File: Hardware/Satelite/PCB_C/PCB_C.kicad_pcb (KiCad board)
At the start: 2 copper layers, 54 x 54 mm, 54 parts, among them IC1 MCP1501T-33E_CHY, IC2 IS25LP080D-JULE-TR, IC3 BQ24392RSER, IC4 MS563702BA03-50, IC5 BMX055, J1 Conn_01x06, J2 BOOT, J3 Conector_PCB_B-C, J4 Conector_Expansion_CanSat, J5 USB_B_Micro, M1 Spacer, M2 Spacer, M3 Spacer, Q1 BC817, U1 NTB0104BQ,115, U2 TCA9802DGKR, U3 STM32F303RETx, U4 NTB0104BQ,115, U5 SN74LVC1G3157DCKR, U6 Si7006-A20-IM1, Y1 LFXTAL016178, Y2 Crystal

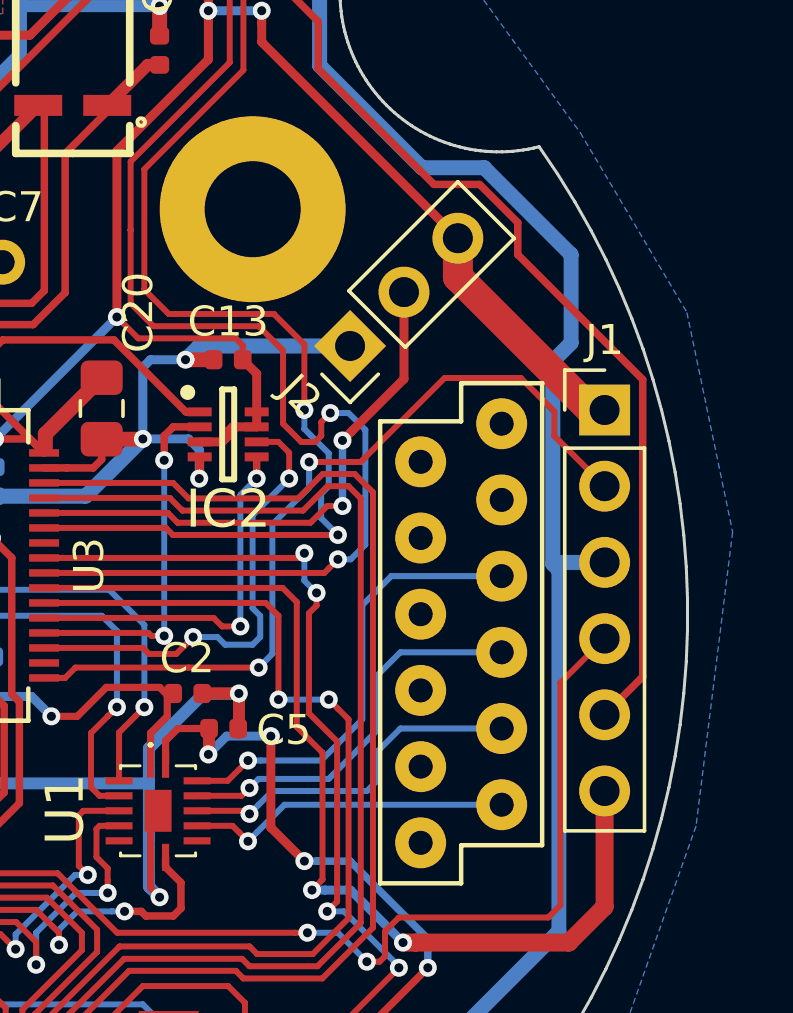
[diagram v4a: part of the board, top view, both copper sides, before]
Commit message: Header de programacion y BOOT de PCB pasados a bottom
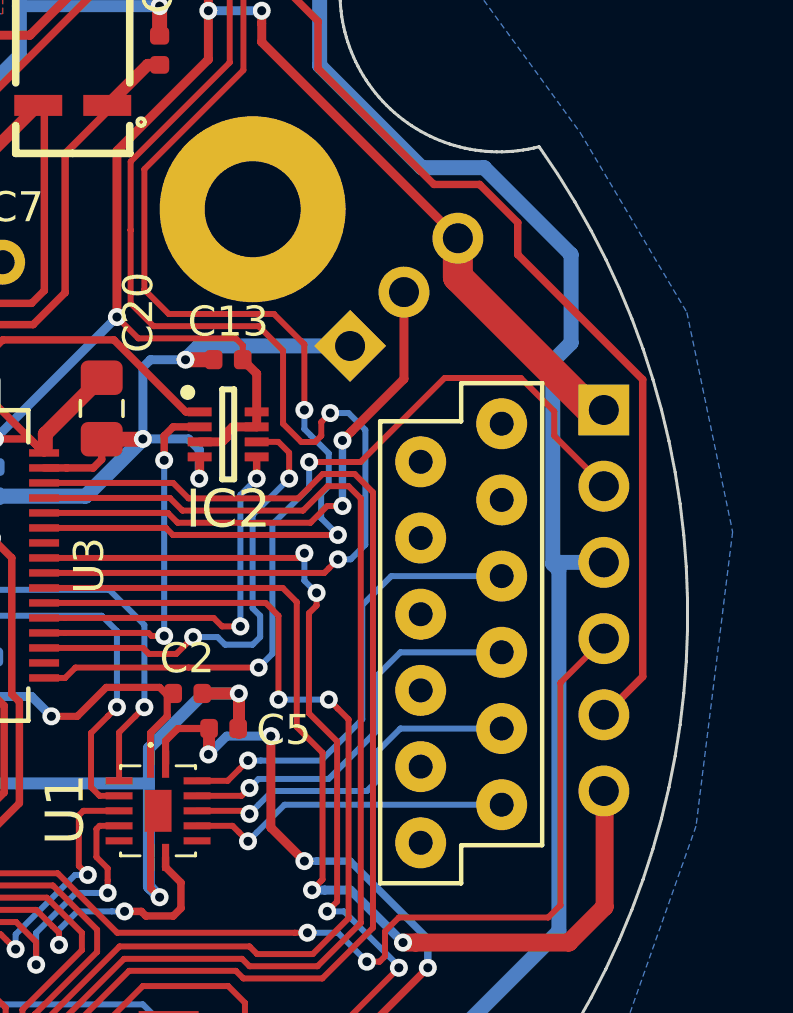
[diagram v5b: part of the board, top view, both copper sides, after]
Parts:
- J1, J2: moved to B.Cu
- turned J1 to 180 degrees
- turned J2 to 315 degrees
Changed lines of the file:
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@@
       (net 27 /IMU/ACC_INT))
   )
-  (module Connector_PinHeader_2.54mm:PinHeader_1x06_P2.54mm_Vertical (layer F.Cu)
-    (at 24.2316 -6.8072)
+  (module Connector_PinHeader_2.54mm:PinHeader_1x06_P2.54mm_Vertical (layer B.Cu)
+    (at 24.2062 -6.8072 180)
     (descr "Through hole straight pin header, 1x06, 2.54mm pitch, single row")
     (tags "Through hole pin header THT 1x06 2.54mm single row")
-    (fp_text reference J1 (at 0 -2.33) (layer F.SilkS)
-      (effects (font (size 1 1) (thickness 0.15)))
+    (fp_text reference J1 (at 0 2.33 180) (layer B.SilkS)
+      (effects (font (size 1 1) (thickness 0.15)) (justify mirror))
     )
-    (fp_text value Conn_01x06 (at 0 15.03) (layer F.Fab)
-      (effects (font (size 1 1) (thickness 0.15)))
+    (fp_text value Conn_01x06 (at 0 -15.03 180) (layer B.Fab)
+      (effects (font (size 1 1) (thickness 0.15)) (justify mirror))
     )
-    (fp_text user %R (at 0 6.35 90) (layer F.Fab)
-      (effects (font (size 1 1) (thickness 0.15)))
+    (fp_text user %R (at 0 -6.35 90) (layer B.Fab)
+      (effects (font (size 1 1) (thickness 0.15)) (justify mirror))
     )
-    (fp_line (start 1.8 -1.8) (end -1.8 -1.8) (layer F.CrtYd) (width 0.05))
-    (fp_line (start 1.8 14.5) (end 1.8 -1.8) (layer F.CrtYd) (width 0.05))
-    (fp_line (start -1.8 14.5) (end 1.8 14.5) (layer F.CrtYd) (width 0.05))
-    (fp_line (start -1.8 -1.8) (end -1.8 14.5) (layer F.CrtYd) (width 0.05))
-    (fp_line (start -1.33 -1.33) (end 0 -1.33) (layer F.SilkS) (width 0.12))
-    (fp_line (start -1.33 0) (end -1.33 -1.33) (layer F.SilkS) (width 0.12))
-    (fp_line (start -1.33 1.27) (end 1.33 1.27) (layer F.SilkS) (width 0.12))
-    (fp_line (start 1.33 1.27) (end 1.33 14.03) (layer F.SilkS) (width 0.12))
-    (fp_line (start -1.33 1.27) (end -1.33 14.03) (layer F.SilkS) (width 0.12))
-    (fp_line (start -1.33 14.03) (end 1.33 14.03) (layer F.SilkS) (width 0.12))
-    (fp_line (start -1.27 -0.635) (end -0.635 -1.27) (layer F.Fab) (width 0.1))
-    (fp_line (start -1.27 13.97) (end -1.27 -0.635) (layer F.Fab) (width 0.1))
-    (fp_line (start 1.27 13.97) (end -1.27 13.97) (layer F.Fab) (width 0.1))
-    (fp_line (start 1.27 -1.27) (end 1.27 13.97) (layer F.Fab) (width 0.1))
-    (fp_line (start -0.635 -1.27) (end 1.27 -1.27) (layer F.Fab) (width 0.1))
-    (pad 6 thru_hole oval (at 0 12.7) (size 1.7 1.7) (drill 1) (layers *.Cu *.Mask)
+    (fp_line (start 1.8 1.8) (end -1.8 1.8) (layer B.CrtYd) (width 0.05))
+    (fp_line (start 1.8 -14.5) (end 1.8 1.8) (layer B.CrtYd) (width 0.05))
+    (fp_line (start -1.8 -14.5) (end 1.8 -14.5) (layer B.CrtYd) (width 0.05))
+    (fp_line (start -1.8 1.8) (end -1.8 -14.5) (layer B.CrtYd) (width 0.05))
+    (fp_line (start -1.33 1.33) (end 0 1.33) (layer B.SilkS) (width 0.12))
+    (fp_line (start -1.33 0) (end -1.33 1.33) (layer B.SilkS) (width 0.12))
+    (fp_line (start -1.33 -1.27) (end 1.33 -1.27) (layer B.SilkS) (width 0.12))
+    (fp_line (start 1.33 -1.27) (end 1.33 -14.03) (layer B.SilkS) (width 0.12))
+    (fp_line (start -1.33 -1.27) (end -1.33 -14.03) (layer B.SilkS) (width 0.12))
+    (fp_line (start -1.33 -14.03) (end 1.33 -14.03) (layer B.SilkS) (width 0.12))
+    (fp_line (start -1.27 0.635) (end -0.635 1.27) (layer B.Fab) (width 0.1))
+    (fp_line (start -1.27 -13.97) (end -1.27 0.635) (layer B.Fab) (width 0.1))
+    (fp_line (start 1.27 -13.97) (end -1.27 -13.97) (layer B.Fab) (width 0.1))
+    (fp_line (start 1.27 1.27) (end 1.27 -13.97) (layer B.Fab) (width 0.1))
+    (fp_line (start -0.635 1.27) (end 1.27 1.27) (layer B.Fab) (width 0.1))
+    (pad 6 thru_hole oval (at 0 -12.7 180) (size 1.7 1.7) (drill 1) (layers *.Cu *.Mask)
       (net 39 /SWO))
-    (pad 5 thru_hole oval (at 0 10.16) (size 1.7 1.7) (drill 1) (layers *.Cu *.Mask)
+    (pad 5 thru_hole oval (at 0 -10.16 180) (size 1.7 1.7) (drill 1) (layers *.Cu *.Mask)
       (net 7 /NRST))
-    (pad 4 thru_hole oval (at 0 7.62) (size 1.7 1.7) (drill 1) (layers *.Cu *.Mask)
+    (pad 4 thru_hole oval (at 0 -7.62 180) (size 1.7 1.7) (drill 1) (layers *.Cu *.Mask)
       (net 38 /SWDIO))
-    (pad 3 thru_hole oval (at 0 5.08) (size 1.7 1.7) (drill 1) (layers *.Cu *.Mask)
+    (pad 3 thru_hole oval (at 0 -5.08 180) (size 1.7 1.7) (drill 1) (layers *.Cu *.Mask)
       (net 1 GND))
-    (pad 2 thru_hole oval (at 0 2.54) (size 1.7 1.7) (drill 1) (layers *.Cu *.Mask)
+    (pad 2 thru_hole oval (at 0 -2.54 180) (size 1.7 1.7) (drill 1) (layers *.Cu *.Mask)
       (net 37 /SWCLK))
-    (pad 1 thru_hole rect (at 0 0) (size 1.7 1.7) (drill 1) (layers *.Cu *.Mask)
+    (pad 1 thru_hole rect (at 0 0 180) (size 1.7 1.7) (drill 1) (layers *.Cu *.Mask)
       (net 3 +3V3_Internal))
     (model ${KISYS3DMOD}/Connector_PinHeader_2.54mm.3dshapes/PinHeader_1x06_P2.54mm_Vertical.wrl
@@
     )
   )
-  (module Connector_PinHeader_2.54mm:PinHeader_1x03_P2.54mm_Vertical (layer F.Cu)
-    (at 15.748 -8.9408 135)
+  (module Connector_PinHeader_2.54mm:PinHeader_1x03_P2.54mm_Vertical (layer B.Cu)
+    (at 15.748 -8.9408 315)
     (descr "Through hole straight pin header, 1x03, 2.54mm pitch, single row")
     (tags "Through hole pin header THT 1x03 2.54mm single row")
-    (fp_text reference J2 (at 0 -2.33 135) (layer F.SilkS)
-      (effects (font (size 1 1) (thickness 0.15)))
+    (fp_text reference J2 (at 0 2.33 315) (layer B.SilkS)
+      (effects (font (size 1 1) (thickness 0.15)) (justify mirror))
     )
-    (fp_text value BOOT (at 0 7.41 135) (layer F.Fab)
-      (effects (font (size 1 1) (thickness 0.15)))
+    (fp_text value BOOT (at 0 -7.41 315) (layer B.Fab)
+      (effects (font (size 1 1) (thickness 0.15)) (justify mirror))
     )
-    (fp_text user %R (at 0 2.54 225) (layer F.Fab)
-      (effects (font (size 1 1) (thickness 0.15)))
+    (fp_text user %R (at 0 -2.54 225) (layer B.Fab)
+      (effects (font (size 1 1) (thickness 0.15)) (justify mirror))
     )
-    (fp_line (start 1.8 -1.8) (end -1.8 -1.8) (layer F.CrtYd) (width 0.05))
-    (fp_line (start 1.8 6.85) (end 1.8 -1.8) (layer F.CrtYd) (width 0.05))
-    (fp_line (start -1.8 6.85) (end 1.8 6.85) (layer F.CrtYd) (width 0.05))
-    (fp_line (start -1.8 -1.8) (end -1.8 6.85) (layer F.CrtYd) (width 0.05))
-    (fp_line (start -1.33 -1.33) (end 0 -1.33) (layer F.SilkS) (width 0.12))
-    (fp_line (start -1.33 0) (end -1.33 -1.33) (layer F.SilkS) (width 0.12))
-    (fp_line (start -1.33 1.27) (end 1.33 1.27) (layer F.SilkS) (width 0.12))
-    (fp_line (start 1.33 1.27) (end 1.33 6.41) (layer F.SilkS) (width 0.12))
-    (fp_line (start -1.33 1.27) (end -1.33 6.41) (layer F.SilkS) (width 0.12))
-    (fp_line (start -1.33 6.41) (end 1.33 6.41) (layer F.SilkS) (width 0.12))
-    (fp_line (start -1.27 -0.635) (end -0.635 -1.27) (layer F.Fab) (width 0.1))
-    (fp_line (start -1.27 6.35) (end -1.27 -0.635) (layer F.Fab) (width 0.1))
-    (fp_line (start 1.27 6.35) (end -1.27 6.35) (layer F.Fab) (width 0.1))
-    (fp_line (start 1.27 -1.27) (end 1.27 6.35) (layer F.Fab) (width 0.1))
-    (fp_line (start -0.635 -1.27) (end 1.27 -1.27) (layer F.Fab) (width 0.1))
-    (pad 3 thru_hole oval (at 0 5.079999 135) (size 1.7 1.7) (drill 1) (layers *.Cu *.Mask)
+    (fp_line (start 1.8 1.8) (end -1.8 1.8) (layer B.CrtYd) (width 0.05))
+    (fp_line (start 1.8 -6.85) (end 1.8 1.8) (layer B.CrtYd) (width 0.05))
+    (fp_line (start -1.8 -6.85) (end 1.8 -6.85) (layer B.CrtYd) (width 0.05))
+    (fp_line (start -1.8 1.8) (end -1.8 -6.85) (layer B.CrtYd) (width 0.05))
+    (fp_line (start -1.33 1.33) (end 0 1.33) (layer B.SilkS) (width 0.12))
+    (fp_line (start -1.33 0) (end -1.33 1.33) (layer B.SilkS) (width 0.12))
+    (fp_line (start -1.33 -1.27) (end 1.33 -1.27) (layer B.SilkS) (width 0.12))
+    (fp_line (start 1.33 -1.27) (end 1.33 -6.41) (layer B.SilkS) (width 0.12))
+    (fp_line (start -1.33 -1.27) (end -1.33 -6.41) (layer B.SilkS) (width 0.12))
+    (fp_line (start -1.33 -6.41) (end 1.33 -6.41) (layer B.SilkS) (width 0.12))
+    (fp_line (start -1.27 0.635) (end -0.635 1.27) (layer B.Fab) (width 0.1))
+    (fp_line (start -1.27 -6.35) (end -1.27 0.635) (layer B.Fab) (width 0.1))
+    (fp_line (start 1.27 -6.35) (end -1.27 -6.35) (layer B.Fab) (width 0.1))
+    (fp_line (start 1.27 1.27) (end 1.27 -6.35) (layer B.Fab) (width 0.1))
+    (fp_line (start -0.635 1.27) (end 1.27 1.27) (layer B.Fab) (width 0.1))
+    (pad 3 thru_hole oval (at 0 -5.079999 315) (size 1.7 1.7) (drill 1) (layers *.Cu *.Mask)
       (net 3 +3V3_Internal))
-    (pad 2 thru_hole oval (at 0 2.54 135) (size 1.7 1.7) (drill 1) (layers *.Cu *.Mask)
+    (pad 2 thru_hole oval (at 0 -2.54 315) (size 1.7 1.7) (drill 1) (layers *.Cu *.Mask)
       (net 40 "Net-(J2-Pad2)"))
-    (pad 1 thru_hole rect (at 0 0 135) (size 1.7 1.7) (drill 1) (layers *.Cu *.Mask)
+    (pad 1 thru_hole rect (at 0 0 315) (size 1.7 1.7) (drill 1) (layers *.Cu *.Mask)
       (net 1 GND))
     (model ${KISYS3DMOD}/Connector_PinHeader_2.54mm.3dshapes/PinHeader_1x03_P2.54mm_Vertical.wrl

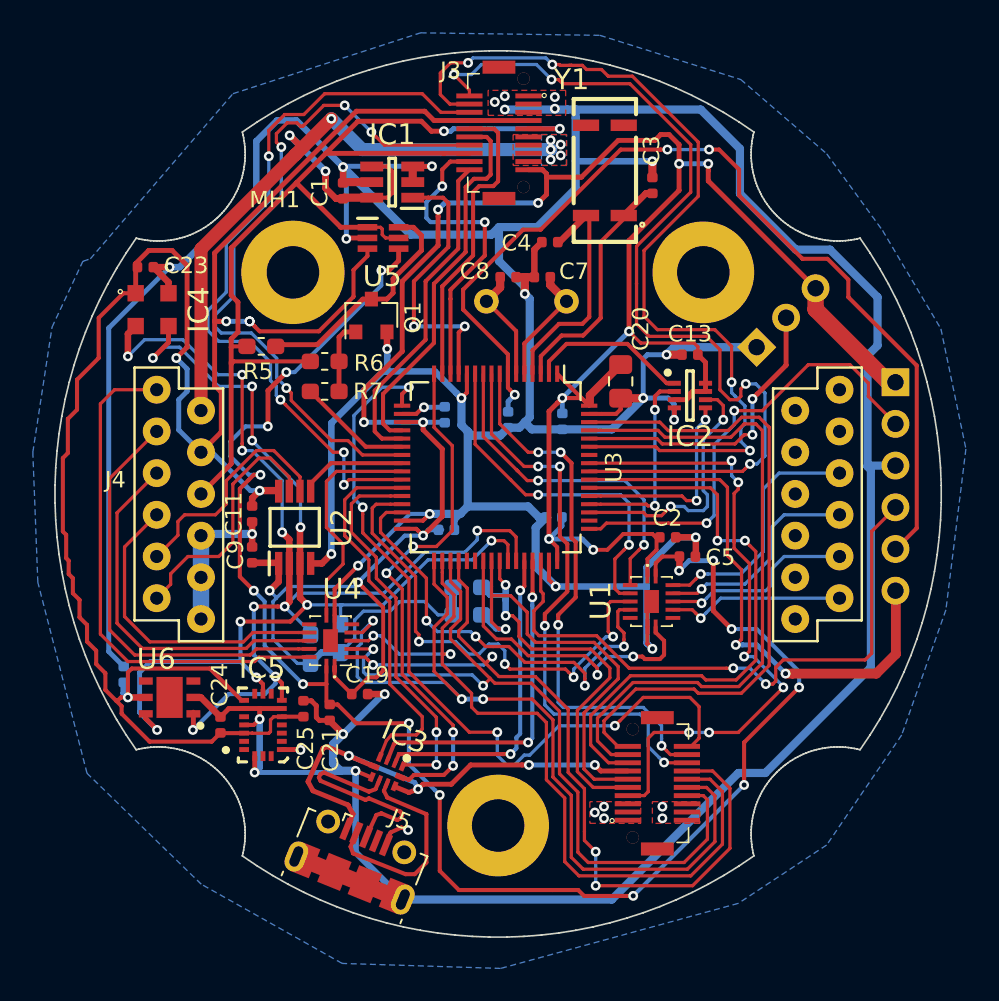
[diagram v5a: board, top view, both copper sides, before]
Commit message: Eliminado switch de 5V y 3.3V y corrección en pines de SPI al CC1101 en PCB_C
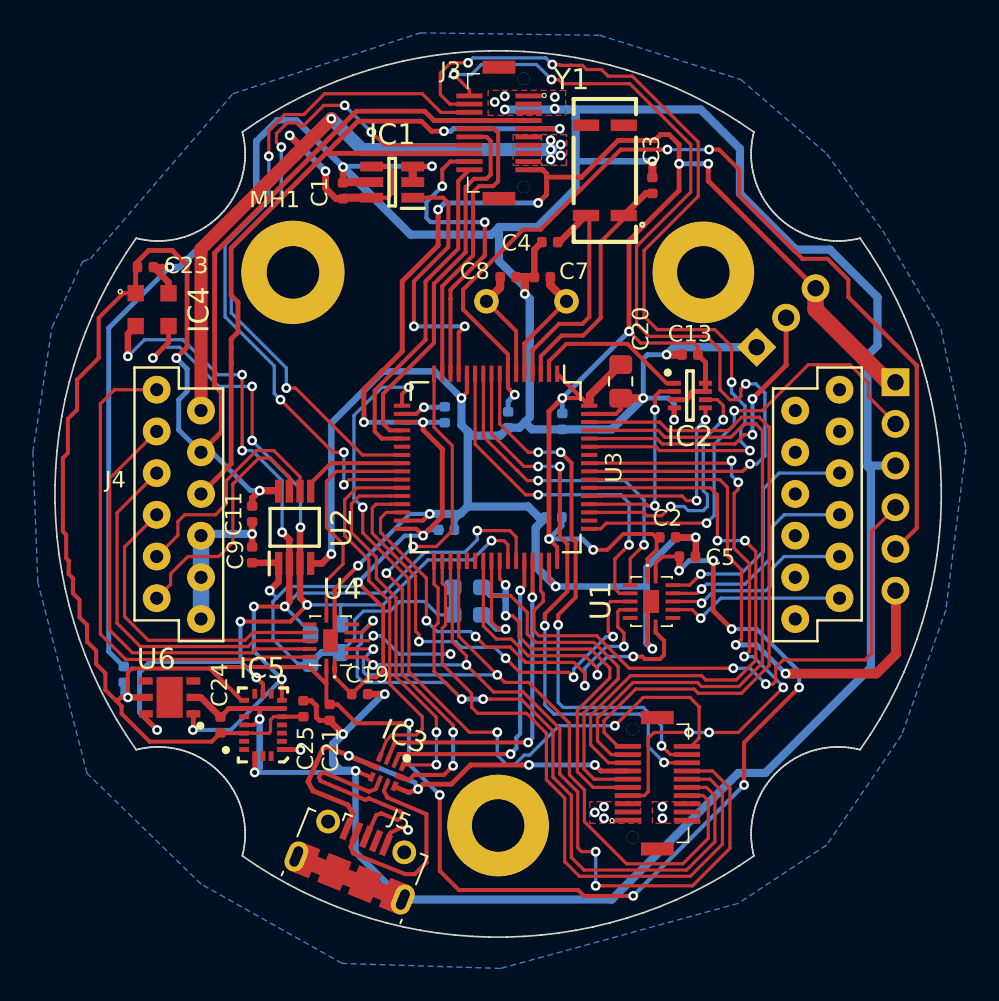
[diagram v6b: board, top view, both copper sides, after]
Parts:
- removed Q1: BC817, Package_TO_SOT_SMD:SOT-23
- removed R5: 10k, Resistor_SMD:R_0603_1608Metric_Pad1.05x0.95mm_HandSolder
- removed R6: 100k, Resistor_SMD:R_0603_1608Metric_Pad1.05x0.95mm_HandSolder
- removed R7: 1k, Resistor_SMD:R_0603_1608Metric_Pad1.05x0.95mm_HandSolder
- removed U5: SN74LVC1G3157DCKR, SamacSys_Parts:SOT65P210X110-6N
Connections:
- C21 pad 1: VDD -> +3V3
- C5 pad 1: VDD -> +3V3
- U1 pad 14: VDD -> +3V3
- U3 pad 22: /SWITCH_IO_V -> Net-(U3-Pad22)
- U3 pad 35: /SDI -> /SDO
- U3 pad 36: /SDO -> /SDI
- U4 pad 14: VDD -> +3V3
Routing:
- net VDD: track 100.3 -> 0.00 mm, vias 14 -> 0
- net +3V3: track 128.4 -> 186.3 mm, vias 6 -> 11
- net Net-(Q1-Pad3): track 14.0 -> 0.00 mm
- net +5V: track 64.4 -> 50.4 mm
- net GND: track 367.2 -> 359.1 mm, vias 36 -> 34
- net /SWITCH_IO_V: track 6.99 -> 0.00 mm
- net Net-(Q1-Pad1): track 4.46 -> 0.00 mm
- net /SDI: track 46.5 -> 44.1 mm
- net /SDO: track 50.4 -> 48.0 mm
- net /5V_ENABLE: track 42.8 -> 40.7 mm
- net /3V_ENABLE: track 45.3 -> 43.4 mm
- net /IO2: track 29.8 -> 28.8 mm
- net /CS: track 51.5 -> 50.7 mm
- net /SCLK: track 47.7 -> 46.9 mm

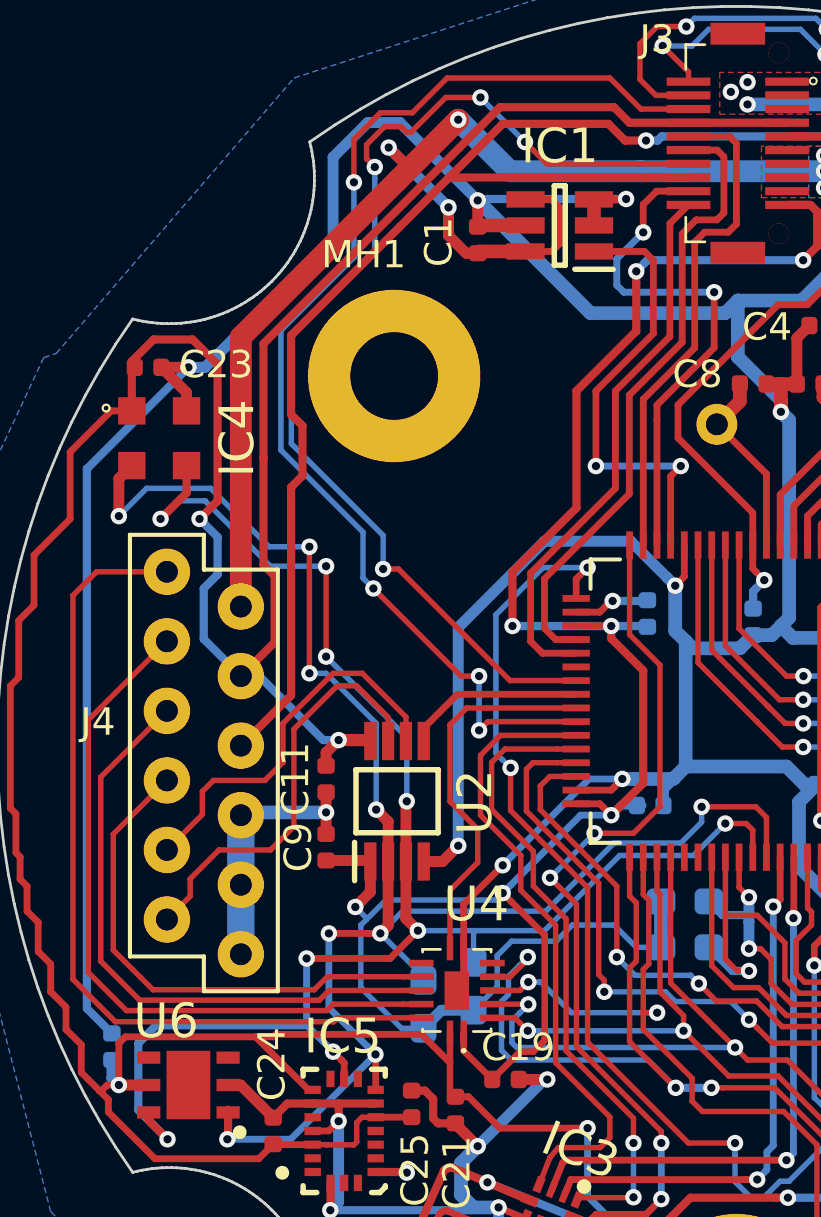
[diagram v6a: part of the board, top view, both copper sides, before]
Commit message: Movidas resistencias de I2C a top en PCB_C
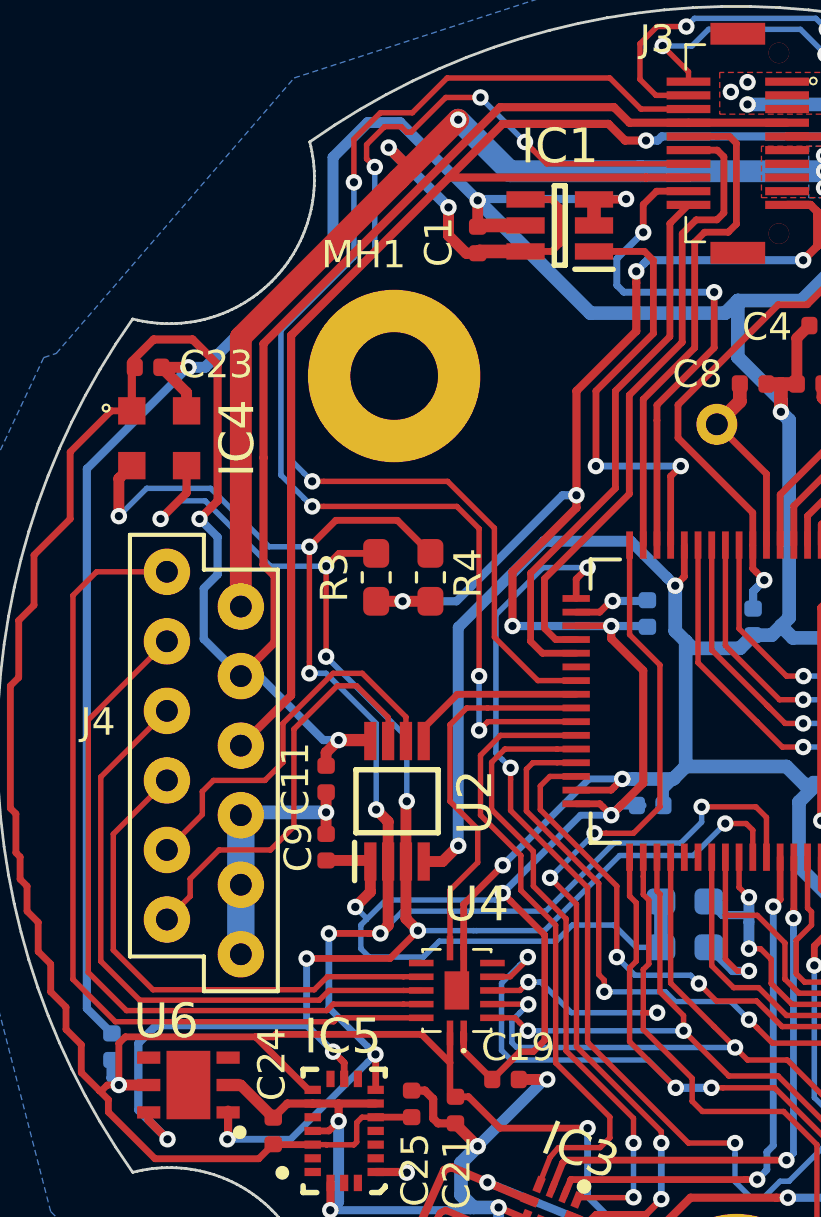
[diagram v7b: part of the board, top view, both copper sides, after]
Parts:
- R3, R4: moved to F.Cu
- moved R4 15.6 mm to (-11.2, -6.15)
- moved R3 15.4 mm to (-13.2, -6.15)
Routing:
- net +3V3_Internal: track 173.7 -> 179.9 mm, vias 13 -> 15
- net /SDA: track 62.9 -> 65.8 mm
- net /3V_ENABLE: track 43.4 -> 46.1 mm
- net /5V_ENABLE: track 40.7 -> 42.6 mm
- net /SCL: track 61.6 -> 62.5 mm
